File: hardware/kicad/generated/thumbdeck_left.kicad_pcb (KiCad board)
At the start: 2 copper layers, 74.5 x 109.5 mm, 84 parts, among them SW1 SNAP7, SW10 SNAP7, SW11 SNAP7, SW12 SNAP7, SW13 SNAP7, SW14 SNAP7, SW15 SNAP7, SW16 SNAP7, SW17 SNAP7, SW18 SNAP7, SW19 SNAP7, SW2 SNAP7, SW20 SNAP7, SW21 SNAP7, SW22 SNAP7, SW23 SNAP7, SW24 SNAP7, SW25 SNAP7, SW26 SNAP7, SW27 SNAP7, SW28 SNAP7, SW29 SNAP7, SW3 SNAP7, SW30 SNAP7, SW31 SNAP7, SW32 SNAP7, SW33 SNAP7, SW34 SNAP7, SW35 SNAP7, SW36 SNAP7, SW37 SNAP7, SW38 SNAP7, SW39 SNAP7, SW4 SNAP7, SW40 SNAP7, SW41 SNAP7, SW42 SNAP7, SW5 SNAP7, SW6 SNAP7, SW7 SNAP7, SW8 SNAP7, SW9 SNAP7

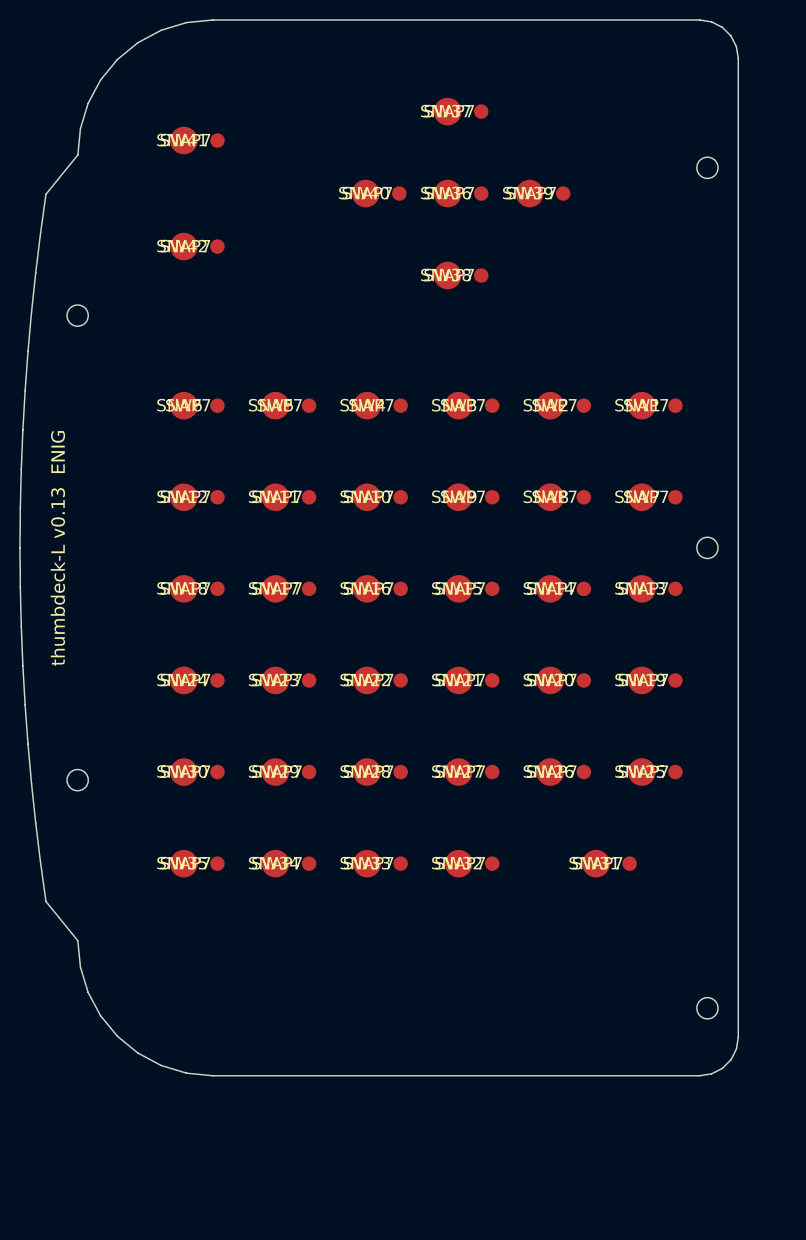
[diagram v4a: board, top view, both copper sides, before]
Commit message: Autonomous route+validate loop working (KiCad 9 + Freerouting)
- Upgraded toolchain: KiCad 9 (drc/render CLI + Specctra API), Freerouting 2.2.4
  (Java 25). gen_board.py places real footprints (Snaptron dome, marbastlib E73,
  stock USB-C/SOT-23/SOD-323/0402) + full netlist; route.sh runs the loop:
  DSN export -> Freerouting autoroute -> SES import -> DRC(json) -> 2D+3D render.
- Solved the headless blockers: Specctra export chokes on the custom dome pad and
  the MountingHole footprint -> use simple circular dome pads + Edge.Cuts holes.
- First autoroute of the right grip: 780 tracks + 100 vias; DRC 34 violations /
  44 unconnected (iterating to clean). E73 pin-map + wiring in docs/routing-status.md.

Co-Authored-By: Claude Opus 4.8 <noreply@anthropic.com>
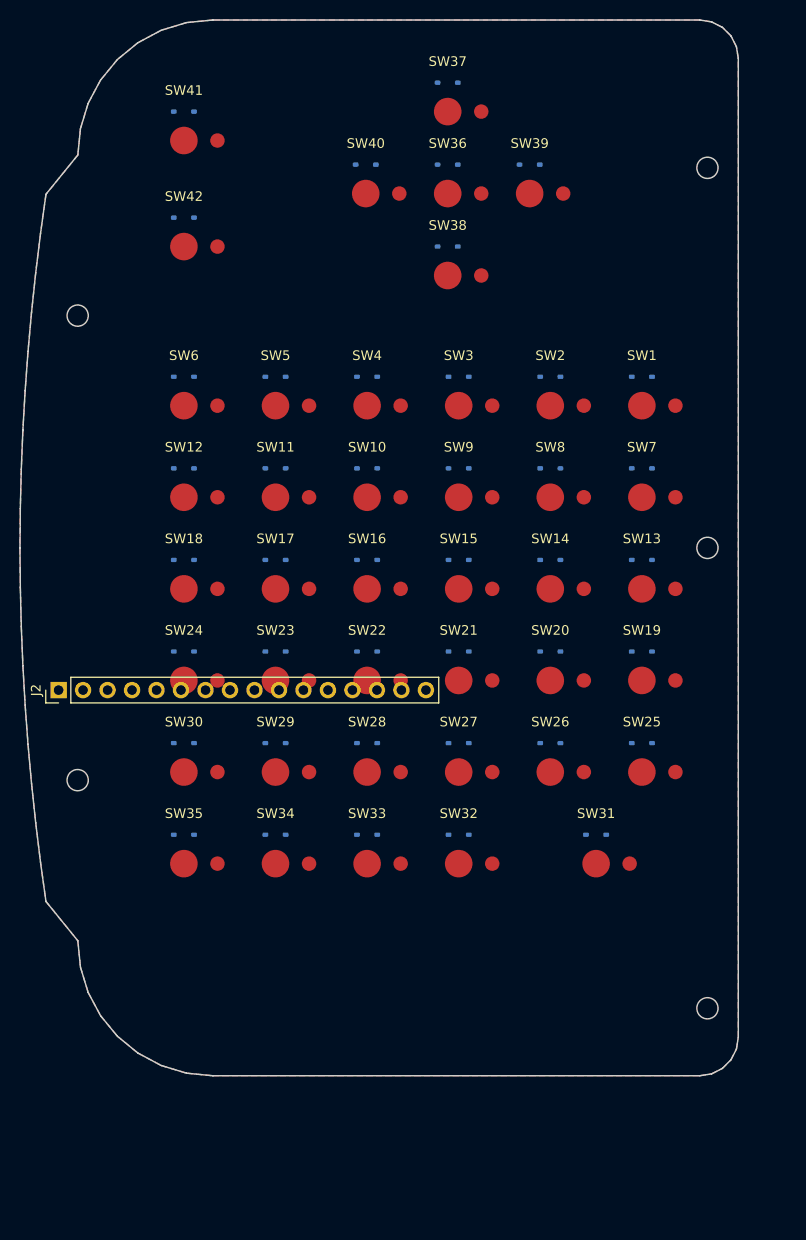
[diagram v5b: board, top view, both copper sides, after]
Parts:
- added J2: BRIDGE_16, PinHeader_1x16_P2.54mm_Vertical, F.Cu at (4.00, 69.5)
- SW1, SW10, SW11, SW12, SW13, SW14, SW15, SW16, SW17, SW18, SW19, SW2, SW20, SW21, SW22, SW23, SW24, SW25, SW26, SW27, SW28, SW29, SW3, SW30, SW31, SW32, SW33, SW34, SW35, SW36, SW37, SW38, SW39, SW4, SW40, SW41, SW42, SW5, SW6, SW7, SW8, SW9: footprint (none) -> snaptron_7mm_simple
- moved D36 2.80 mm to (44.4, 15.0), turned to 180 degrees
- moved D37 2.80 mm to (44.4, 6.50), turned to 180 degrees
- moved D38 2.80 mm to (44.4, 23.5), turned to 180 degrees
- moved D39 2.80 mm to (52.9, 15.0), turned to 180 degrees
- moved D40 2.80 mm to (35.9, 15.0), turned to 180 degrees
- moved D41 2.80 mm to (17.0, 9.50), turned to 180 degrees
- moved D42 2.80 mm to (17.0, 20.5), turned to 180 degrees
- moved D1 2.80 mm to (64.5, 37.0), turned to 180 degrees
- moved D10 2.80 mm to (36.0, 46.5), turned to 180 degrees
- moved D11 2.80 mm to (26.5, 46.5), turned to 180 degrees
- moved D12 2.80 mm to (17.0, 46.5), turned to 180 degrees
- moved D13 2.80 mm to (64.5, 56.0), turned to 180 degrees
- moved D14 2.80 mm to (55.0, 56.0), turned to 180 degrees
- moved D15 2.80 mm to (45.5, 56.0), turned to 180 degrees
- moved D16 2.80 mm to (36.0, 56.0), turned to 180 degrees
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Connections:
- net D_L1 renamed DN_L1
- net D_L10 renamed DN_L10
- net D_L11 renamed DN_L11
- net D_L12 renamed DN_L12
- net D_L13 renamed DN_L13
- net D_L14 renamed DN_L14
- net D_L15 renamed DN_L15
- net D_L16 renamed DN_L16
- net D_L17 renamed DN_L17
- net D_L18 renamed DN_L18
- net D_L19 renamed DN_L19
- net D_L2 renamed DN_L2
- net D_L20 renamed DN_L20
- net D_L21 renamed DN_L21
- net D_L22 renamed DN_L22
- net D_L23 renamed DN_L23
- net D_L24 renamed DN_L24
- net D_L25 renamed DN_L25
- net D_L26 renamed DN_L26
- net D_L27 renamed DN_L27
- net D_L28 renamed DN_L28
- net D_L29 renamed DN_L29
- net D_L3 renamed DN_L3
- net D_L30 renamed DN_L30
- net D_L31 renamed DN_L31
- net D_L32 renamed DN_L32
- net D_L33 renamed DN_L33
- net D_L34 renamed DN_L34
- net D_L35 renamed DN_L35
- net D_L36 renamed DN_L36
- net D_L37 renamed DN_L37
- net D_L38 renamed DN_L38
- net D_L39 renamed DN_L39
- net D_L4 renamed DN_L4
- net D_L40 renamed DN_L40
- net D_L41 renamed DN_L41
- net D_L42 renamed DN_L42
- net D_L5 renamed DN_L5
- net D_L6 renamed DN_L6
- net D_L7 renamed DN_L7
- net D_L8 renamed DN_L8
- net D_L9 renamed DN_L9
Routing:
- added copper zone on B.Cu, net GND
- added copper zone on F.Cu, net GND
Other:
- board text removed: "BRIDGE"
- board text removed: "ROUTING + MODULE/CONN FOOTPRINTS = NEXT GATE"
- board text removed: "thumbdeck-L v0.13 ENIG"

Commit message: v0.14: verified-correct 4-layer board, real firmware, 3D shells/keymats + fit-check
PCB / electrical (audited vs datasheets + adversarial multi-lens review):
- FIX blocker: USBLC6-2SC6 ESD shorted USB D+ to D- (pin6 == pin1 node). Rewire
  D+=pins1&6, D-=pins3&4 per ST datasheet.
- Verified E73 pinmap 1:1 vs the official Ebyte datasheet (the "silent killer" is clean).
- Charger R24 2k->5k1 (~505mA -> ~196mA, ~0.5C of a 400mAh cell).
- Fix left-grip bridge header on wrong edge; rotate left-grip switch pads (ring-pad
  direction) so they clear the inner connector.
- Single-sided back assembly: move all reflow parts to B.Cu; connectors J2/J3 to back
  so they clear the top shell + keymat.
- Move bridge cols COL6-9 off the module inner pads to castellated edge pads; cluster
  USB-C/ESD/charger by the module (short D+/D-); add VBAT bulk cap.
- Convert to 4-layer (F/GND-plane/signal/B): RF ground reference + routable fan-in.
- Both grips pass placement DRC clean (0 non-silk violations).

Simulation: sim_matrix.py proves the 79-key col2row matrix is ghosting-free across
~68.5k finger-press scenarios (0 failures; no-diode control ghosts ~35k -> sim is real).

Firmware: replace the stale 50-key nice!nano shield with a generated E73 (nRF52840)
board -- 9x10, 79 keys, real nRF pins + transform/keymap derived from the PCB model
(gen_firmware.py) so hardware and firmware can't drift.

3D CAD (docs/cad-process.md): deck3d.py builds, from the SAME deck.py model, the PCB
fit-model (real component dims), one-piece back shell, front shell (79 key openings +
phone window), keymats, and the LiPo/flex/phone/MagSafe -- assembled + collision-checked
to 0 impossible overlaps (the loop caught+fixed a battery-through-floor + front-connector
clashes). STL/STEP in hardware/cad/models/; renders added.

Docs: authoritative docs/evaluation.md; superseded banners on drifted docs; README gets
3D renders + updated reproduce/routing notes. Trackpad deferred for v1.

Remaining gates: finish the 4-laye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
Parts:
- J2: footprint PinHeader_1x16_P2.54mm_Vertical -> PinHeader_2x08_P2.54mm_Vertical; moved to B.Cu
- moved J2 65.8 mm to (69.5, 75.5), turned to 180 degrees
- turned SW1 to 180 degrees
- turned SW10 to 180 degrees
- turned SW11 to 180 degrees
- turned SW12 to 180 degrees
- turned SW13 to 180 degrees
- turned SW14 to 180 degrees
- turned SW15 to 180 degrees
- turned SW16 to 180 degrees
- turned SW17 to 180 degrees
- turned SW18 to 180 degrees
- turned SW19 to 180 degrees
- turned SW2 to 180 degrees
- turned SW20 to 180 degrees
- turned SW21 to 180 degrees
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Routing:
- added copper zone on In1.Cu, net GND
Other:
- copper layers 2 -> 4

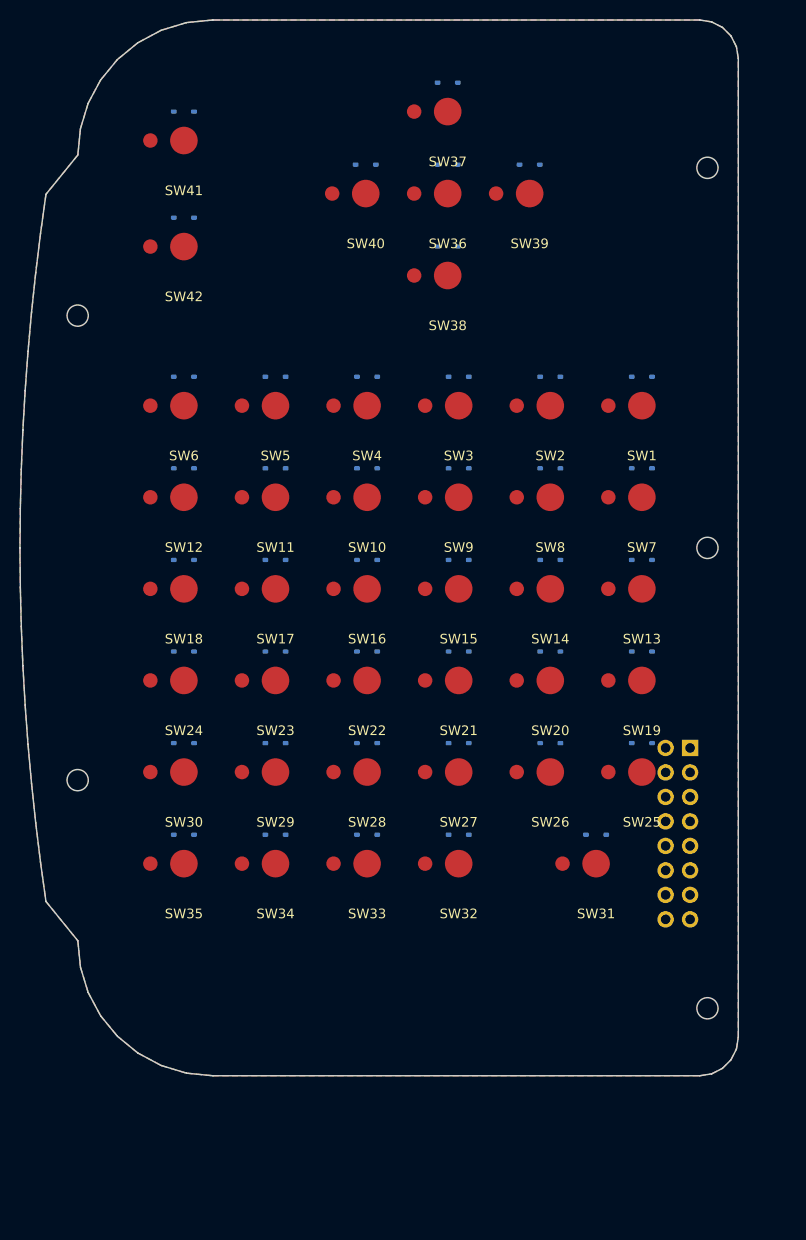
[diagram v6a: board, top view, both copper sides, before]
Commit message: rev-A (v0.15): production-ready boards, fab package, firmware, shells
Full top-to-bottom redesign pass driven by an 8-dimension adversarial audit
(120 findings, 14 blockers) and closed by a 6-agent verification review.

Boards (both DRC 0 violations / 0 unconnected, kicad-cli 9.0.9):
- Production snap-dome footprint: centre pad + 292° leg ring with 67.5° escape
  gap, mask apertures, pour + all-layer via keep-outs (old 2-pad proxy gave
  dead keys at 45° dome rotation)
- E73 rotated antenna-down at the bottom edge; keep-out verified copper-free
- Bridge: 16P 1.0mm FFC ZIF (AFA07-S16FCC-00) per grip + straight type-A
  jumper; left-grip nets assigned by ribbon geometry (proven 1:1)
- Battery: JST-PH SMT + MSK12C02 power switch (charger stays on cell side);
  reset tact (floor pinhole); charge LED on STAT; charger caps at the chip;
  SAADC filter cap; USB ESD inline; deterministic USB data-pair copper
  (interleaved pad pairs are un-autoroutable); COL9 off XL1 to P0.04;
  spare I2C broken out; boards grown to 76.5x114.5 (FFC + module-at-edge)
- Autonomous route loop rebuilt: Freerouting -Xss16m, In1 exported as power
  layer, obstacle-aware GND stitcher, generated GND escape vias, DRC-gated
  fab export (gerbers/BOM/CPL per board, JLC format, LCSC stamped)

Firmware (ZMK v0.3.0): 5 build-breakers fixed (west pin, pointing.h, DCDC
symbol, K32SRC_RC — BLE never started without it, nice!nano flash layout),
board moved to config/boards, FN layer gains -/=/Home/End/PrtSc + mouse keys
on the D-pad, self-contained CI workflow.

Mechanical: USB opening on the real connector, phone pocket + MagSafe ring
recess, PCB support posts, keymat clamp rim, switch slot + pinhole + LED
hole, cavity 6.3mm; fit-check 0 collisions with real part geometry.

Docs rewritten to rev-A reality; stale fab artifacts removed; renders
regenerated. Legacy route-finishing scripts retired to legacy/.

Co-Authored-By: Claude Fable 5 <noreply@anthropic.com>
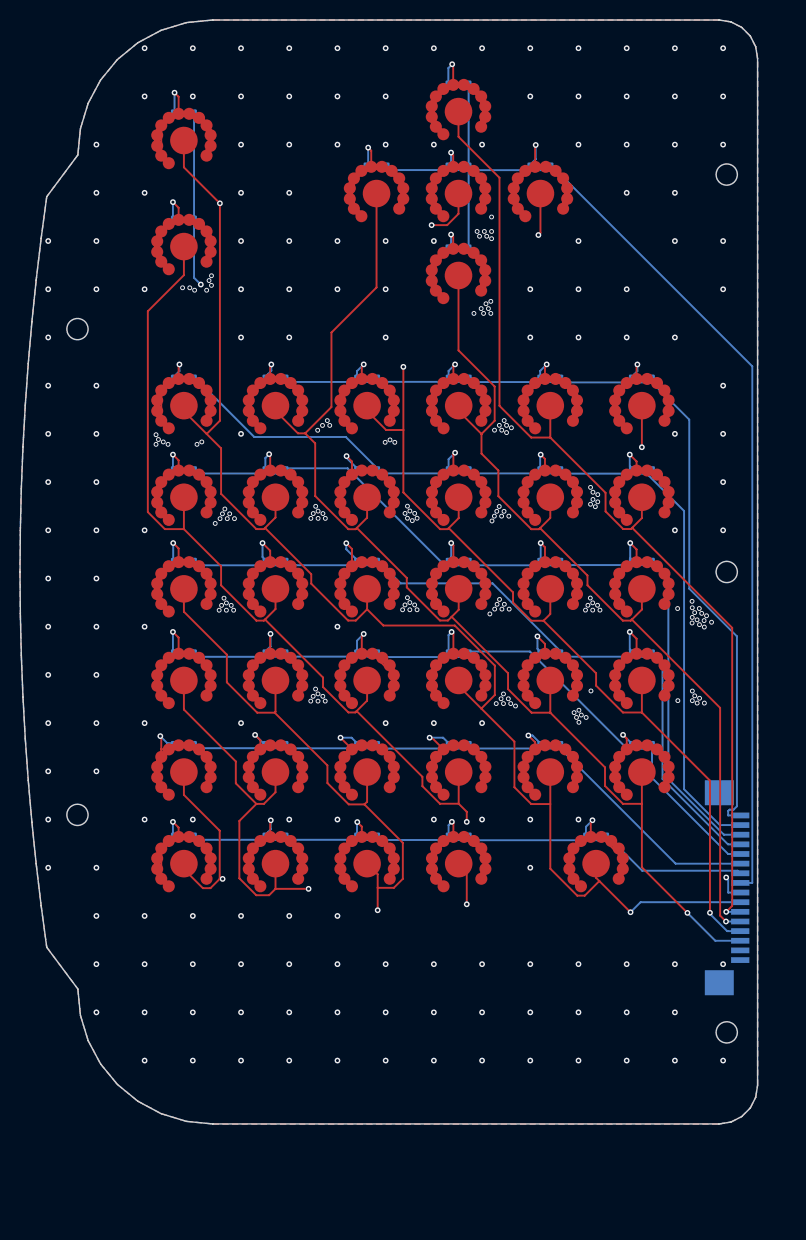
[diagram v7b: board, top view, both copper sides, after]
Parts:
- J2: value BRIDGE_16 -> FFC16; footprint PinHeader_2x08_P2.54mm_Vertical -> ffc_afa07_s16fcc
- SW1, SW10, SW11, SW12, SW13, SW14, SW15, SW16, SW17, SW18, SW19, SW2, SW20, SW21, SW22, SW23, SW24, SW25, SW26, SW27, SW28, SW29, SW3, SW30, SW31, SW32, SW33, SW34, SW35, SW36, SW37, SW38, SW39, SW4, SW40, SW41, SW42, SW5, SW6, SW7, SW8, SW9: footprint snaptron_7mm_simple -> snaptron_7mm_contact
- moved J2 14.9 mm to (72.9, 90.0), turned to 90 degrees
- moved D36 1.12 mm to (45.5, 15.0)
- moved D37 1.12 mm to (45.5, 6.50)
- moved D38 1.12 mm to (45.5, 23.5)
- moved D39 1.12 mm to (54.0, 15.0)
- moved D40 1.12 mm to (37.0, 15.0)
- moved SW36 1.12 mm to (45.5, 18.0), turned to 0 degrees
- moved SW37 1.12 mm to (45.5, 9.50), turned to 0 degrees
- moved SW38 1.12 mm to (45.5, 26.5), turned to 0 degrees
- moved SW39 1.12 mm to (54.0, 18.0), turned to 0 degrees
- moved SW40 1.12 mm to (37.0, 18.0), turned to 0 degrees
- turned SW1 to 0 degrees
- turned SW10 to 0 degrees
- turned SW11 to 0 degrees
- turned SW12 to 0 degrees
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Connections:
- J2 pad 1: ROW0 -> GND
- J2 pad 10: COL5 -> ROW6
- J2 pad 11: COL6 -> ROW5
- J2 pad 12: COL7 -> ROW4
- J2 pad 13: COL8 -> ROW3
- J2 pad 14: COL9 -> ROW2
- J2 pad 15: GND -> ROW1
- J2 pad 16: GND -> ROW0
- J2 pad 2: ROW1 -> GND
- J2 pad 3: ROW2 -> COL9
- J2 pad 4: ROW3 -> COL8
- J2 pad 5: ROW4 -> COL7
- J2 pad 6: ROW5 -> COL6
- J2 pad 7: ROW6 -> COL5
- J2 pad 8: ROW7 -> ROW8
- J2 pad 9: ROW8 -> ROW7
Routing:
- net COL6: track 0.00 -> 238.0 mm, vias 0 -> 3
- net COL5: track 0.00 -> 215.7 mm, vias 0 -> 4
- net COL8: track 0.00 -> 199.3 mm, vias 0 -> 4
- net COL9: track 0.00 -> 191.6 mm, vias 0 -> 2
- net COL7: track 0.00 -> 187.3 mm, vias 0 -> 2
- net ROW7: track 0.00 -> 119.1 mm
- net ROW8: track 0.00 -> 105.2 mm, vias 0 -> 2
- net ROW1: track 0.00 -> 94.5 mm
- net ROW0: track 0.00 -> 90.6 mm
- net ROW2: track 0.00 -> 86.5 mm
- net ROW3: track 0.00 -> 77.4 mm
- net ROW4: track 0.00 -> 69.1 mm
- net ROW5: track 0.00 -> 63.7 mm
- net ROW6: track 0.00 -> 60.1 mm
- net DN_L41: track 0.00 -> 19.4 mm, vias 0 -> 1
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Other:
- board size 74.5 x 109.5 mm -> 76.5 x 114.5 mm
- board text added: "J2 FFC16 <- pin1"
